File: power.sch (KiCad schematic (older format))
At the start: 32 parts

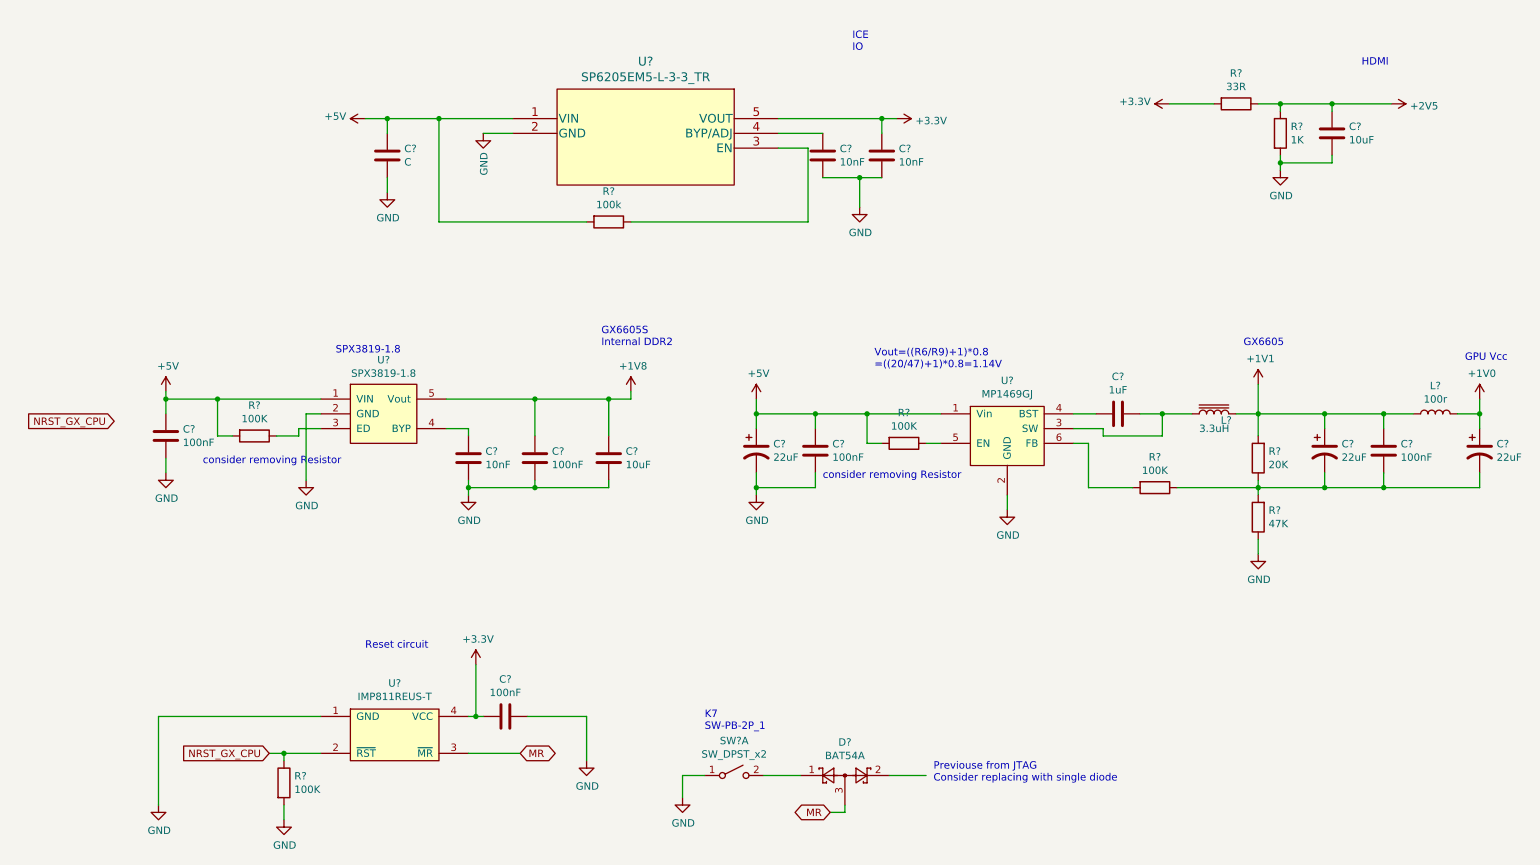
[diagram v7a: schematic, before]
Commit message: broke, out all GPIO and finsihed wiring HDMI
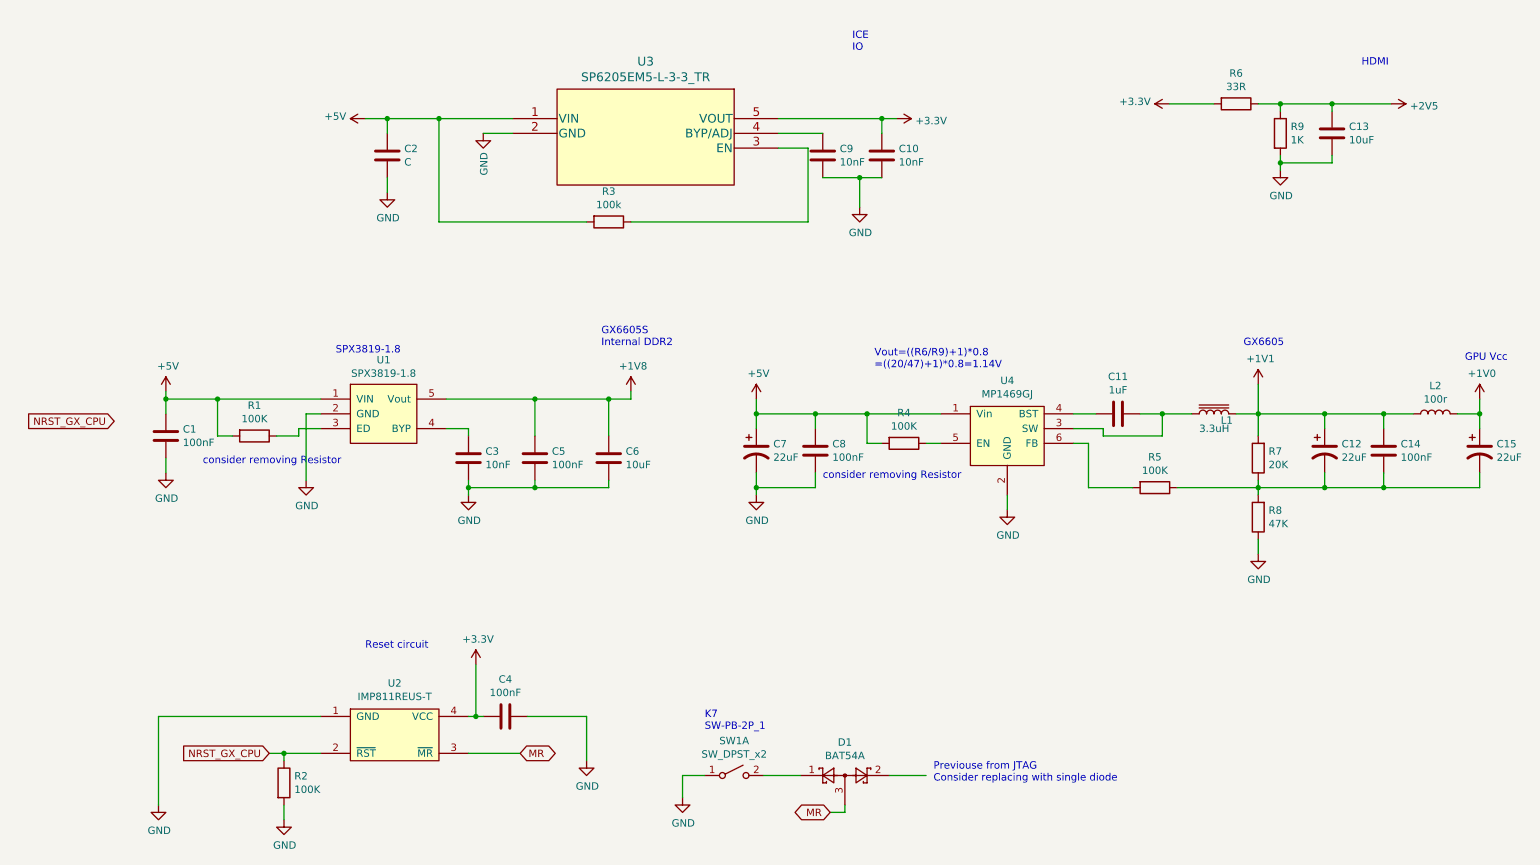
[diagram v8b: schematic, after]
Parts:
- gave numbers to parts that had none: 32
